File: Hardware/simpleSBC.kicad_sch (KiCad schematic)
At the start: 72 parts, among them J1 Conn_02x07_Odd_Even, J3 Conn_02x10_Odd_Even, J5 USB_A, J6 USB_A, J7 RJ45_Wuerth_7499010121A, J9 Conn_02x10_Odd_Even, SW1 SW_Push, U1 STM32MP157FAD1, U2 STMPS2252MTR, U5 USBLC6-4SC6, U6 LAN8742A, X1 ASCO, Y1 32.786, Y3 24M

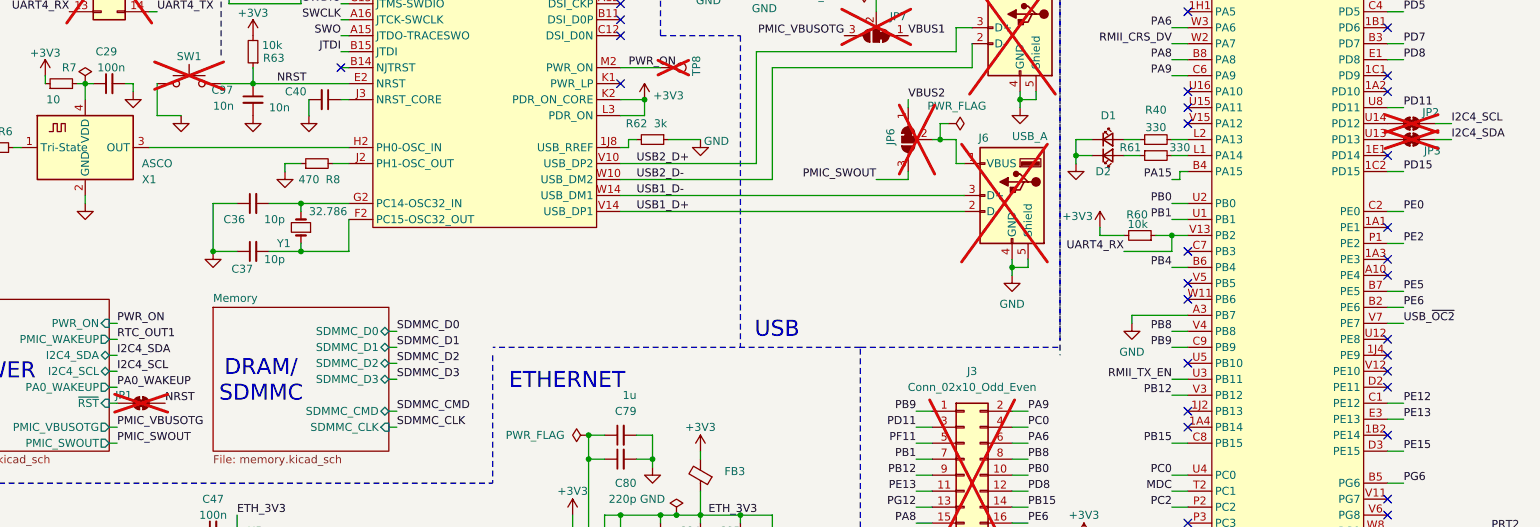
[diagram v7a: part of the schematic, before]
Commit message: Default close jumpers and fix USB signal switching
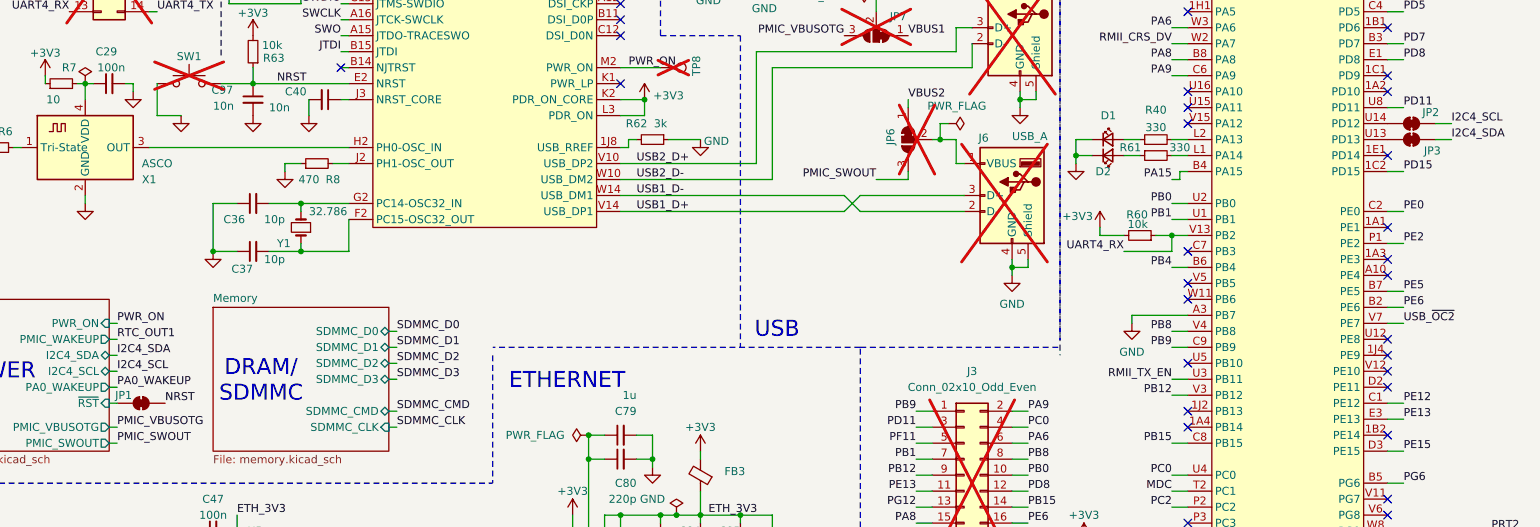
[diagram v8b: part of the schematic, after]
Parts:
- JP1, JP2, JP3: footprint Resistor_SMD:R_0402_1005Metric -> SimpleSBC:Jumper_0402_Short; now fitted; now left out of the parts list
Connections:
- net USB1_D+: now also J6.3 (D+); no longer J6.2 (D-)
- net USB1_D-: now also J6.2 (D-); no longer J6.3 (D+)
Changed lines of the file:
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@@
 	(wire
 		(pts
+			(xy 161.29 68.58) (xy 177.8 68.58)
+		)
+		(stroke
+			(width 0)
+			(type default)
+		)
+	)
+	(wire
+		(pts
 			(xy 146.05 22.86) (xy 148.59 22.86)
 		)
@@
 	(wire
 		(pts
+			(xy 161.29 66.04) (xy 158.75 68.58)
+		)
+		(stroke
+			(width 0)
+			(type default)
+		)
+	)
+	(wire
+		(pts
 			(xy 176.53 43.18) (xy 176.53 39.37)
 		)
@@
 	(wire
 		(pts
+			(xy 158.75 66.04) (xy 161.29 68.58)
+		)
+		(stroke
+			(width 0)
+			(type default)
+		)
+	)
+	(wire
+		(pts
 			(xy 257.81 142.24) (xy 261.62 142.24)
 		)
@@
 	(wire
 		(pts
+			(xy 123.19 66.04) (xy 158.75 66.04)
+		)
+		(stroke
+			(width 0)
+			(type default)
+		)
+	)
+	(wire
+		(pts
 			(xy 53.34 119.38) (xy 55.88 119.38)
 		)
@@
 	(wire
 		(pts
-			(xy 123.19 66.04) (xy 177.8 66.04)
-		)
-		(stroke
-			(width 0)
-			(type default)
-		)
-	)
-	(wire
-		(pts
 			(xy 118.11 107.95) (xy 118.11 129.54)
 		)
@@
 	(wire
 		(pts
-			(xy 123.19 68.58) (xy 177.8 68.58)
-		)
-		(stroke
-			(width 0)
-			(type default)
-		)
-	)
-	(wire
-		(pts
 			(xy 57.15 158.75) (xy 57.15 163.83)
 		)
@@
 	(wire
 		(pts
+			(xy 177.8 66.04) (xy 161.29 66.04)
+		)
+		(stroke
+			(width 0)
+			(type default)
+		)
+	)
+	(wire
+		(pts
 			(xy 58.42 67.31) (xy 58.42 74.93)
 		)
@@
 	(wire
 		(pts
+			(xy 123.19 68.58) (xy 158.75 68.58)
+		)
+		(stroke
+			(width 0)
+			(type default)
+		)
+	)
+	(wire
+		(pts
 			(xy 170.18 102.87) (xy 172.72 102.87)
 		)
@@
 		(unit 1)
 		(exclude_from_sim no)
-		(in_bom yes)
+		(in_bom no)
 		(on_board yes)
-		(dnp yes)
+		(dnp no)
 		(property "Reference" "JP2"
 			(at 251.968 52.832 0)
@@
 			)
 		)
-		(property "Footprint" "Resistor_SMD:R_0402_1005Metric"
+		(property "Footprint" "SimpleSBC:Jumper_0402_Short"
 			(at 248.92 54.61 0)
 			(effects
@@
 		(unit 1)
 		(exclude_from_sim no)
-		(in_bom yes)
+		(in_bom no)
 		(on_board yes)
-		(dnp yes)
+		(dnp no)
 		(property "Reference" "JP1"
 			(at 44.196 97.79 0)
@@
 			)
 		)
-		(property "Footprint" "Resistor_SMD:R_0402_1005Metric"
+		(property "Footprint" "SimpleSBC:Jumper_0402_Short"
 			(at 46.99 99.06 0)
 			(effects
@@
 		(unit 1)
 		(exclude_from_sim no)
-		(in_bom yes)
+		(in_bom no)
 		(on_board yes)
-		(dnp yes)
+		(dnp no)
 		(property "Reference" "JP3"
 			(at 252.222 58.928 0)
@@
 			)
 		)
-		(property "Footprint" "Resistor_SMD:R_0402_1005Metric"
+		(property "Footprint" "SimpleSBC:Jumper_0402_Short"
 			(at 248.92 57.15 0)
 			(effects
